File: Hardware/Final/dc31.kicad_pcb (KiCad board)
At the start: 2 copper layers, 109.7 x 112.5 mm, 59 parts, among them J1 Micro_SD_Card_SPI, J2 MIDI IN, J3 MIDI OUT, J4 OLED, J5 SYNC OUT, J6 SYNC IN, J7 HEADPHONE, Q1 3904, SW1 SW_Push, SW10 SW_Push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

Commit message: Schematic is pretty much complete.  Back board is 90% routed.
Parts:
- removed R12: 10k, Resistor_SMD:R_0603_1608Metric
- removed the R5 at (172.9, 18.5)
- removed REF**: Speaker, lib_fp:Speaker
- removed SW20, SW21: Rotary, lib_fp:RotaryEncoder
- added C2: 10uF, Capacitor_SMD:C_0805_2012Metric, F.Cu at (100.0, 96.1)
- added C3: 3.3nF, Capacitor_SMD:C_0805_2012Metric, F.Cu at (101.6, 90.8)
- added C7: 22uF, Capacitor_SMD:C_0805_2012Metric, F.Cu at (105.8, 98.1)
- added D14: D_Schottky, Diode_SMD:D_SOD-323, F.Cu at (111.0, 100.4)
- added D15: D_Schottky, Diode_SMD:D_SOD-323, F.Cu at (197.0, 113.2)
- added J3: FRONT, Connector_PinHeader_2.54mm:PinHeader_1x04_P2.54mm_Vertical, F.Cu at (196.4, 124.6)
- added J7: Eurorack, Connector_IDC:IDC-Header_2x05_P2.54mm_Vertical, B.Cu at (107.2, 117.7)
- added L1: 2.2uH, Inductor_SMD:L_Wuerth_MAPI-3015, F.Cu at (110.0, 97.0)
- added R11: 100k, Resistor_SMD:R_0603_1608Metric, F.Cu at (109.5, 93.0)
- added SW11: Function Select, lib_fp:RotaryEncoder, F.Cu at (123.7, 70.6)
- added SW12: Volume, lib_fp:RotaryEncoder, F.Cu at (142.8, 70.6)
- added SW14: SW_SPDT, lib_fp:SW_SPDT_CK-JS102011SAQN, F.Cu at (204.5, 116.8)
- added TP2: BATT+, TestPoint:TestPoint_Pad_1.5x1.5mm, F.Cu at (202.9, 126.7)
- added TP3: BATT-, TestPoint:TestPoint_Pad_1.5x1.5mm, F.Cu at (202.9, 131.0)
- added U6: TPS62153, Package_DFN_QFN:VQFN-16-1EP_3x3mm_P0.5mm_EP1.68x1.68mm_ThermalVias, F.Cu at (103.8, 94.4)
- C1: renamed from C4; moved to F.Cu
- C4: renamed from C1; moved to F.Cu
- C5: renamed from C2; moved to F.Cu
- C6: renamed from C3; moved to F.Cu
- D1, D10, D11, D12, D2, D3, D4, D5, D6, D7, D8, D9: footprint Diode_SMD:D_SOD-123 -> Diode_SMD:D_SOD-323
- D13: renamed from D14; footprint Diode_SMD:D_SOD-123 -> Diode_SMD:D_SOD-323; moved to F.Cu
- D16: renamed from D13; footprint Diode_SMD:D_SOD-123 -> Diode_SMD:D_SOD-323; moved to F.Cu
- J9: renamed from J1; moved to F.Cu
- Q1, U1, U5: moved to F.Cu
- R1: renamed from R6; moved to F.Cu
- R10: renamed from R2; moved to F.Cu
- R2: renamed from R7; moved to F.Cu
- R3: renamed from R8; moved to F.Cu
- R4: renamed from R9; moved to F.Cu
- R5: renamed from R10; moved to F.Cu
- R6: renamed from R11; moved to F.Cu
- R7: renamed from R1; moved to F.Cu
- R8: renamed from R4; value 220R -> 10R; moved to F.Cu
- R9: renamed from R3; value 220R -> 33R; moved to F.Cu
- SW1: value SW_Push -> Seq1
- SW10: value SW_Push -> Function
- SW2: value SW_Push -> Seq2
- SW3: value SW_Push -> Seq3
- SW4: value SW_Push -> Seq4
- SW5: value SW_Push -> Seq5
- SW6: value SW_Push -> Seq6
- SW7: value SW_Push -> Seq7
- SW8: value SW_Push -> Seq8
- SW9: value SW_Push -> PlayPause
- TP1: renamed from TP3; moved to F.Cu
- TP4: renamed from TP2; moved to F.Cu
- TP5: renamed from TP1; moved to F.Cu
- U2: renamed from U8; moved to F.Cu
- U3: renamed from U2; moved to F.Cu
- U4: renamed from U3; moved to F.Cu
- moved U1 144.8 mm to (180.9, 92.8)
- moved D11 137.8 mm to (123.8, 60.5), turned to 180 degrees
- moved D12 124.9 mm to (142.7, 60.6), turned to 180 degrees
- moved D9 123.7 mm to (123.7, 82.5), turned to 180 degrees
- moved R7 119.9 mm to (164.7, 58.6)
- moved TP5 116.5 mm to (158.3, 62.4), turned to 0 degrees
- moved U3 115.8 mm to (164.0, 63.2)
- moved TP1 115.6 mm to (169.1, 63.4)
- moved SW9 115.6 mm to (123.7, 93.2)
- moved SW10 115.6 mm to (142.8, 93.2)
- moved TP4 112.7 mm to (158.3, 67.4)
- moved J9 111.8 mm to (133.7, 45.4), turned to 180 degrees
- moved D5 108.4 mm to (123.7, 148.9), turned to 180 degrees
- moved D10 108.2 mm to (142.8, 82.5), turned to 180 degrees
- moved D1 104.3 mm to (123.7, 108.4), turned to 180 degrees
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- renumbered J4 to J1, J5 to J2, J6 to J4, J2 to J5, J3 to J6, J7 to J8
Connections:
- C6 pad 1: VBUS -> +3V3
- D10 pad 1: R0 -> R1
- D11 pad 1: R1 -> R2
- D12 pad 1: R2 -> R3
- D13 pad 1: Net-(D14-K) -> Net-(D13-K)
- D4 pad 1: R0 -> R3
- D5 pad 1: R1 -> R0
- D6 pad 1: R2 -> R1
- D7 pad 1: R0 -> R2
- D8 pad 1: R1 -> R3
- D9 pad 1: R2 -> R0
- J8 pad 2: Net-(J7-Pad2) -> Net-(U3-OUTN)
- J8 pad 3: unconnected-(J7-Pad3) -> Net-(U3-OUTN)
- J8 pad 4: Net-(U2-OUTN) -> Net-(J8-Pad4)
- Q1 pad 1: GND -> Net-(D13-K)
- Q1 pad 2: Net-(D14-K) -> GND
- R5 pad 2: Net-(D14-K) -> Net-(D13-K)
- R7 pad 1: VBUS -> +3V3
- R9 pad 2: VBUS -> +3V3
- SW10 pad 1: C3 -> C2
- SW4 pad 1: C1 -> C0
- SW7 pad 1: C2 -> C1
- SW8 pad 1: C2 -> C1
- TP5 pad 1: Net-(J7-Pad2) -> Net-(J8-Pad4)
- U1 pad 19: SCL -> SDA
- U1 pad 20: SDA -> SCL
- U1 pad 24: R2 -> C2
- U1 pad 25: R1 -> unconnected-(U1-GPIO19-Pad25)
- U1 pad 27: C3 -> R1
- U1 pad 29: C2 -> R2
- U1 pad 34: RGB_IN -> R3
- U1 pad 39: unconnected-(U1-VSYS-Pad39) -> VCC
- U1 pad 40: VBUS -> unconnected-(U1-VBUS-Pad40)
- U1 pad 5: unconnected-(U1-GPIO3-Pad5) -> RGB
- U2 pad 7: VBUS -> VCC
- U2 pad 8: VBUS -> VCC
- U3 pad 10: Net-(U2-OUTN) -> Net-(U3-OUTN)
- U3 pad 7: VBUS -> +3V3
- U3 pad 8: VBUS -> +3V3
- U4 pad 14: VBUS -> +3V3
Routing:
- net C1: track 8.65 -> 140.7 mm, vias 0 -> 2
- net R0: track 0.00 -> 129.8 mm, vias 0 -> 3
- net R1: track 0.00 -> 113.6 mm, vias 0 -> 3
- net C2: track 5.77 -> 119.1 mm, vias 0 -> 3
- net C0: track 8.78 -> 106.5 mm, vias 0 -> 1
- net SDA: track 0.00 -> 81.1 mm, vias 0 -> 1
- net SCL: track 0.00 -> 73.9 mm, vias 0 -> 1
- net R2: track 0.00 -> 66.6 mm, vias 0 -> 2
- net SD_CS: track 0.00 -> 63.9 mm, vias 0 -> 2
- net SD_MOSI: track 0.00 -> 62.4 mm, vias 0 -> 2
- net SD_SCK: track 0.00 -> 62.1 mm, vias 0 -> 2
- net R3: track 0.00 -> 61.3 mm, vias 0 -> 2
- net SD_MISO: track 0.00 -> 57.5 mm, vias 0 -> 2
- net GND: track 5.50 -> 61.0 mm, vias 0 -> 27
- net I2S_LRCLK: track 6.66 -> 56.8 mm, vias 0 -> 2
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- added copper zone on B.Cu, net GND
- added copper zone on F.Cu, net GND
- added copper zone on F.Cu, net Net-(L1-Pad1)
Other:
- board size 109.7 x 112.5 mm -> 109.7 x 109.5 mm
- board text added: "@hamster@fosstodon.org"
- board text removed: "@hamster"
- board text removed: "MIDI In"
- board text removed: "MIDI Out"
- board text removed: "Sync In"
- board text removed: "Sync Out"

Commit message: Almost final, still need some artwork
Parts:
- TP2, TP3: moved to B.Cu
- moved J3 15.1 mm to (197.1, 139.7)
- moved SW14 1.75 mm to (202.7, 116.8)
- moved D15 1.73 mm to (195.2, 113.2)
- turned TP2 to 180 degrees
- turned TP3 to 180 degrees
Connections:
- U1 pad 21: ENC2_B -> ENC1_A
- U1 pad 22: ENC2_A -> ENC1_B
- U1 pad 6: ENC1_A -> ENC2_A
- U1 pad 7: ENC1_B -> ENC2_B
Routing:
- net +3V3: track 12.8 -> 219.4 mm, vias 0 -> 8
- net VCC: track 16.3 -> 172.6 mm, vias 0 -> 2
- net R2: track 66.6 -> 151.5 mm
- net R3: track 61.3 -> 138.5 mm
- net ENC2_A: track 0.00 -> 66.7 mm, vias 0 -> 1
- net RGB: track 0.00 -> 66.0 mm, vias 0 -> 1
- net ENC2_B: track 0.00 -> 57.3 mm, vias 0 -> 1
- net ENC1_A: track 0.00 -> 56.9 mm, vias 0 -> 2
- net ENC1_B: track 0.00 -> 54.4 mm, vias 0 -> 2
- net C1: track 140.7 -> 126.8 mm
- net +5V: track 9.43 -> 22.3 mm
- net GND: track 61.0 -> 65.7 mm
- net SD_MISO: track 57.5 -> 56.4 mm
- net Net-(J6-Pad3): track 23.2 -> 22.3 mm
- net Net-(SW14-B): track 16.1 -> 16.9 mm, vias 0 -> 1
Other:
- outline, holes or cut-outs redrawn
- board text added: "-12V GND GND GND +12V"
- board text added: "Audio"
- board text added: "MIDI In"
- board text added: "MIDI Out"
- board text added: "OFF"
- board text added: "ON"
- board text added: "Speaker"
- board text added: "Sync In"
- board text added: "Sync Out"

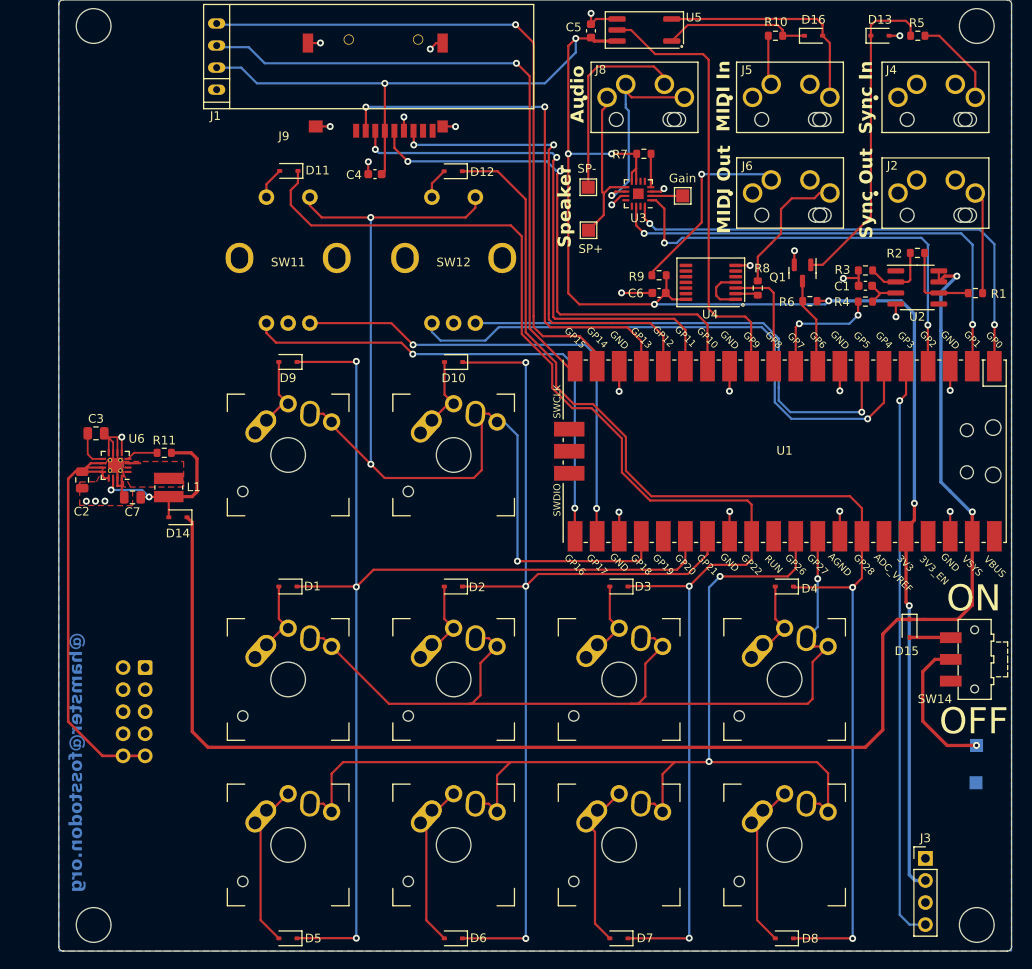
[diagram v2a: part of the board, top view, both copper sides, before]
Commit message: Adding SAO port to front panel Adding hamster art to boards A few more small tweaks before final export
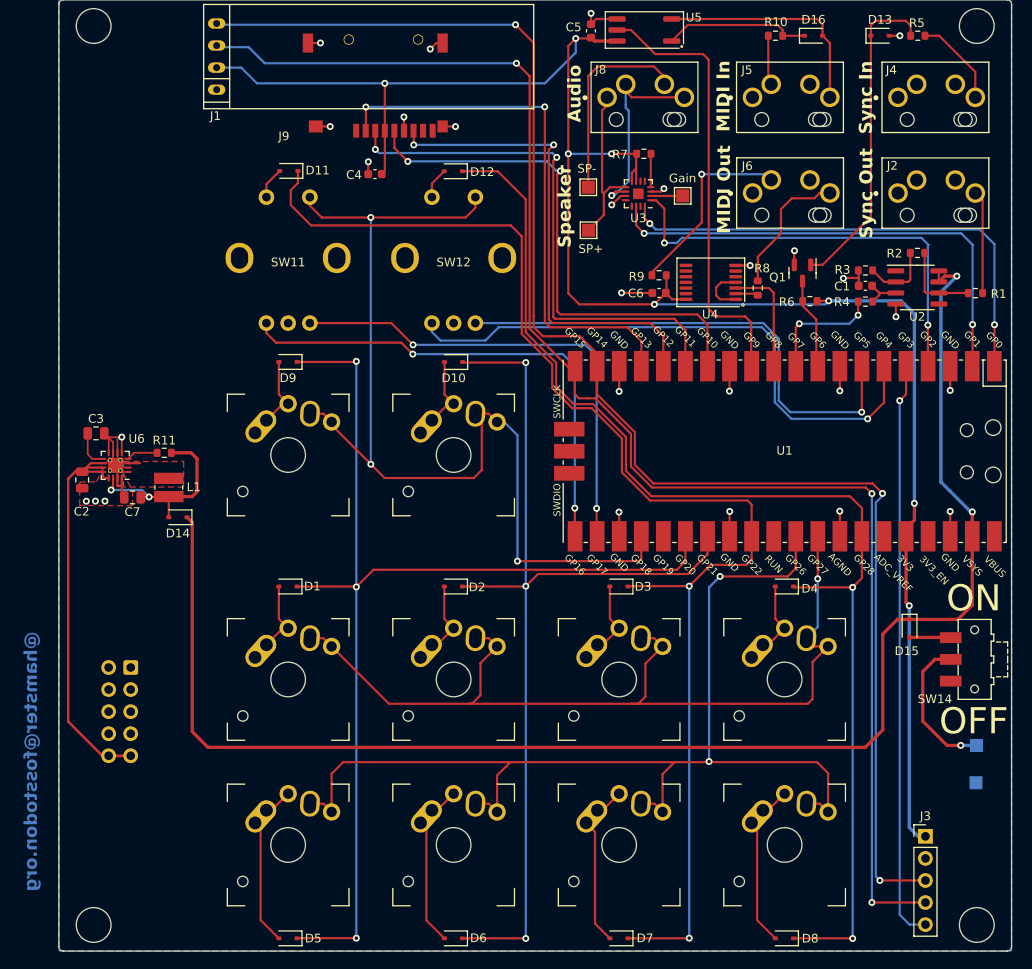
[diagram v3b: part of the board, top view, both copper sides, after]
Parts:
- J3: footprint Connector_PinHeader_2.54mm:PinHeader_1x04_P2.54mm_Vertical -> Connector_PinHeader_2.54mm:PinHeader_1x05_P2.54mm_Vertical
- moved J3 2.54 mm to (197.1, 137.1)
- moved J7 1.66 mm to (105.6, 117.7)
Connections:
- J3 pad 1: GND -> +3V3
- J3 pad 2: +3V3 -> GND
- J3 pad 3: unconnected-(J3-Pin_3-Pad3) -> SDA
- J3 pad 4: RGB -> SCL
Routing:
- net SCL: track 73.9 -> 170.6 mm, vias 1 -> 3
- net SDA: track 81.1 -> 173.5 mm, vias 1 -> 3
- net +3V3: track 219.4 -> 214.1 mm
- net +12V: track 49.3 -> 46.8 mm

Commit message: Final files as submitted to fab
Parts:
- added G***: LOGO, lib_fp:ZiaLogo, B.Cu at (181.3, 93.6)
- added G***: LOGO, lib_fp:DCZiaElectricSampler, B.Cu at (179.9, 71.7)
- added G***: LOGO, lib_fp:hamster, B.Cu at (104.4, 58.8)
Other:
- board text added: "Design by DCZia Team 2023"
- board text added: "github.com/dczia/Defcon31-Badge"

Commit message: Generated 1.1 rev to switch to KYCON 3.5mm jacks due to parts issues with the Molex
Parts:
- J2, J4, J5, J6, J8: footprint lib_fp:MOLEX_47257-0001 -> lib_fp:STX-3790-5N
- moved J2 5.23 mm to (199.1, 62.2)
- moved J4 5.23 mm to (199.1, 51.2)
- moved J6 5.23 mm to (182.3, 62.2)
- moved J8 5.23 mm to (165.6, 51.2)
- moved J5 5.23 mm to (182.3, 51.2)
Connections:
- J2 pad 1: GND -> unconnected-(J2-Pad1)
- J2 pad 2: Net-(J2-Pad2) -> unconnected-(J2-Pad2)
- J2 pad 4: unconnected-(J2-Pad4) -> Net-(J2-Pad4)
- J4 pad 1: GND -> unconnected-(J4-Pad1)
- J4 pad 2: Net-(J4-Pad2) -> unconnected-(J4-Pad2)
- J4 pad 4: unconnected-(J4-Pad4) -> Net-(J4-Pad4)
- J5 pad 1: unconnected-(J5-Pad1) -> Net-(J5-Pad1)
- J5 pad 2: Net-(D16-A) -> unconnected-(J5-Pad2)
- J5 pad 3: Net-(J5-Pad3) -> unconnected-(J5-Pad3)
- J5 pad 4: unconnected-(J5-Pad4) -> Net-(D16-A)
- J6 pad 1: GND -> Net-(J6-Pad1)
- J6 pad 2: Net-(J6-Pad2) -> unconnected-(J6-Pad2)
- J6 pad 3: Net-(J6-Pad3) -> unconnected-(J6-Pad3)
- J6 pad 4: unconnected-(J6-Pad4) -> Net-(J6-Pad4)
- J8 pad 1: Net-(U3-OUTP) -> Net-(U3-OUTN)
- J8 pad 2: Net-(U3-OUTN) -> unconnected-(J8-Pad2)
- J8 pad 3: Net-(U3-OUTN) -> Net-(J8-Pad3)
- J8 pad 4: Net-(J8-Pad4) -> Net-(U3-OUTN)
- R1 pad 1: Net-(J2-Pad2) -> Net-(J2-Pad4)
- R10 pad 1: Net-(J5-Pad3) -> Net-(J5-Pad1)
- R5 pad 1: Net-(J4-Pad2) -> Net-(J4-Pad4)
- R8 pad 1: Net-(J6-Pad2) -> Net-(J6-Pad4)
- R9 pad 1: Net-(J6-Pad3) -> Net-(J6-Pad1)
- TP5 pad 1: Net-(J8-Pad4) -> Net-(J8-Pad3)
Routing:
- net Net-(J8-Pad4): track 23.4 -> 0.00 mm
- net Net-(J6-Pad3): track 22.3 -> 0.00 mm, vias 1 -> 0
- net Net-(J8-Pad3): track 0.00 -> 19.3 mm, vias 0 -> 2
- net Net-(J6-Pad1): track 0.00 -> 18.8 mm, vias 0 -> 1
- net Net-(J6-Pad2): track 15.8 -> 0.00 mm
- net Net-(J6-Pad4): track 0.00 -> 15.5 mm
- net Net-(J2-Pad4): track 0.00 -> 13.8 mm
- net Net-(J2-Pad2): track 11.9 -> 0.00 mm
- net Net-(J4-Pad2): track 10.4 -> 0.00 mm
- net Net-(J4-Pad4): track 0.00 -> 8.81 mm
- net Net-(J5-Pad1): track 0.00 -> 8.05 mm
- net Net-(J5-Pad3): track 5.73 -> 0.00 mm
- net Net-(U3-OUTP): track 19.2 -> 21.1 mm
- net Net-(D16-A): track 26.3 -> 25.3 mm
- net Net-(U3-OUTN): track 23.6 -> 24.4 mm
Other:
- board text added: "Rev 1.1"
